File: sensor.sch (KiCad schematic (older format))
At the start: 91 parts, among them CON1 Micro USB, CON2 PROG, CON3 Jack-DC, CON4 HTU21D, CON5 Conn_01x08, Q1 BSS214N, Q2 BSS214N, Q3 BSS214N, Q4 BSS214N, Q5 BSS214N, Q6 BSS214N, SW1 RESET, SW2 CFG, U1 LM7805, U2 TLV1117LV33DCY, U3 ESP-12F, U4 HTU21D, U5 PMS7003

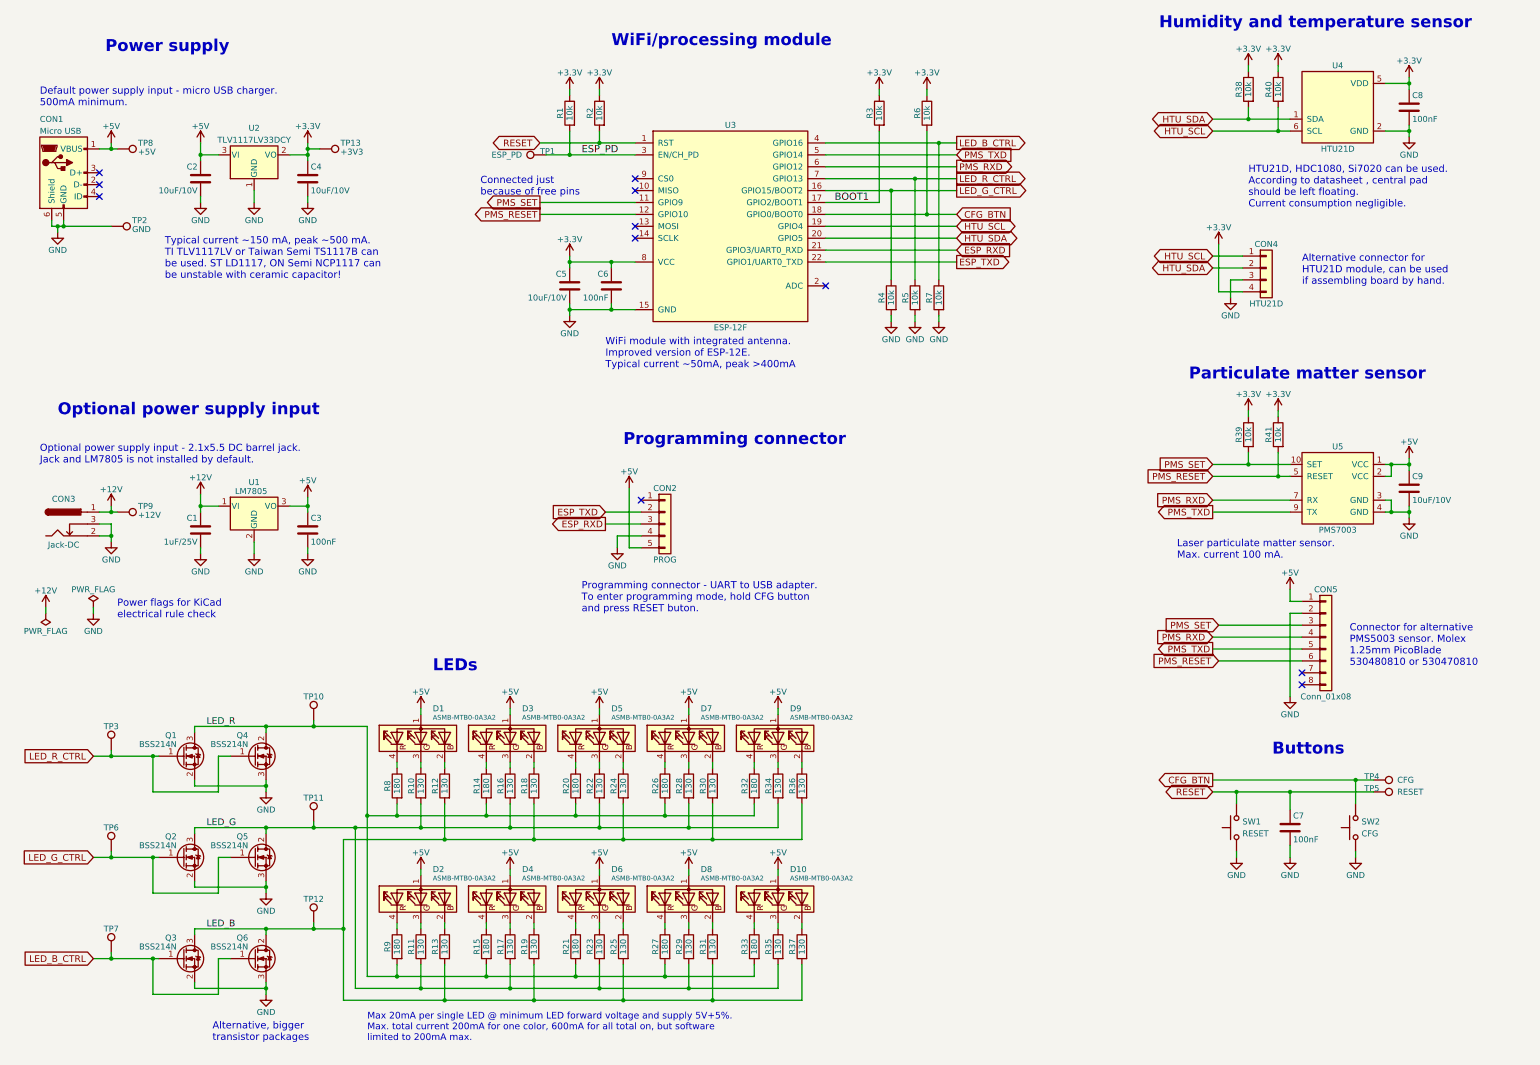
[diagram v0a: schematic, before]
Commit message: Add HTU21D module footprint
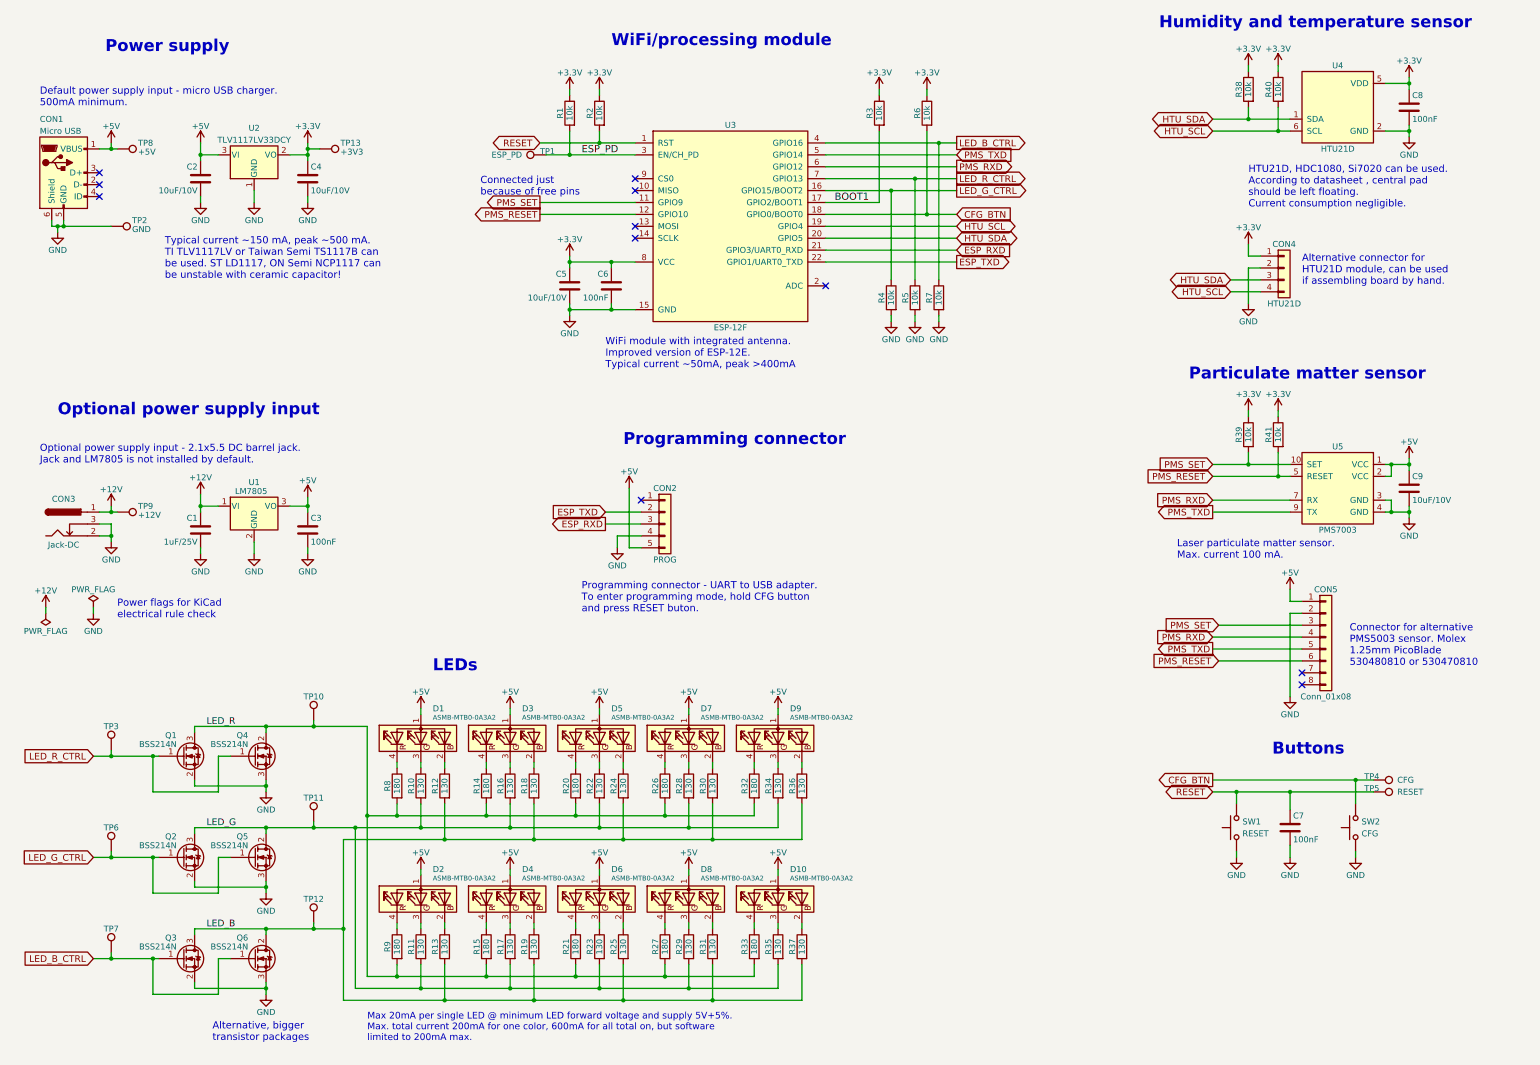
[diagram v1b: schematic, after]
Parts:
- CON4: footprint Pin_Headers:Pin_Header_Straight_1x04_Pitch2.54mm -> less-smog:HTU21D_module
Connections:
- net +3V3: now also CON4.1 (Pin_1); no longer CON4.4 (Pin_4)
- net GND: now also CON4.2 (Pin_2); no longer CON4.3 (Pin_3)
- net HTU_SCL: now also CON4.4 (Pin_4); no longer CON4.1 (Pin_1)
- net HTU_SDA: now also CON4.3 (Pin_3); no longer CON4.2 (Pin_2)
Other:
- moved on the sheet: CON4

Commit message: Change some footprints. Optimize routing.
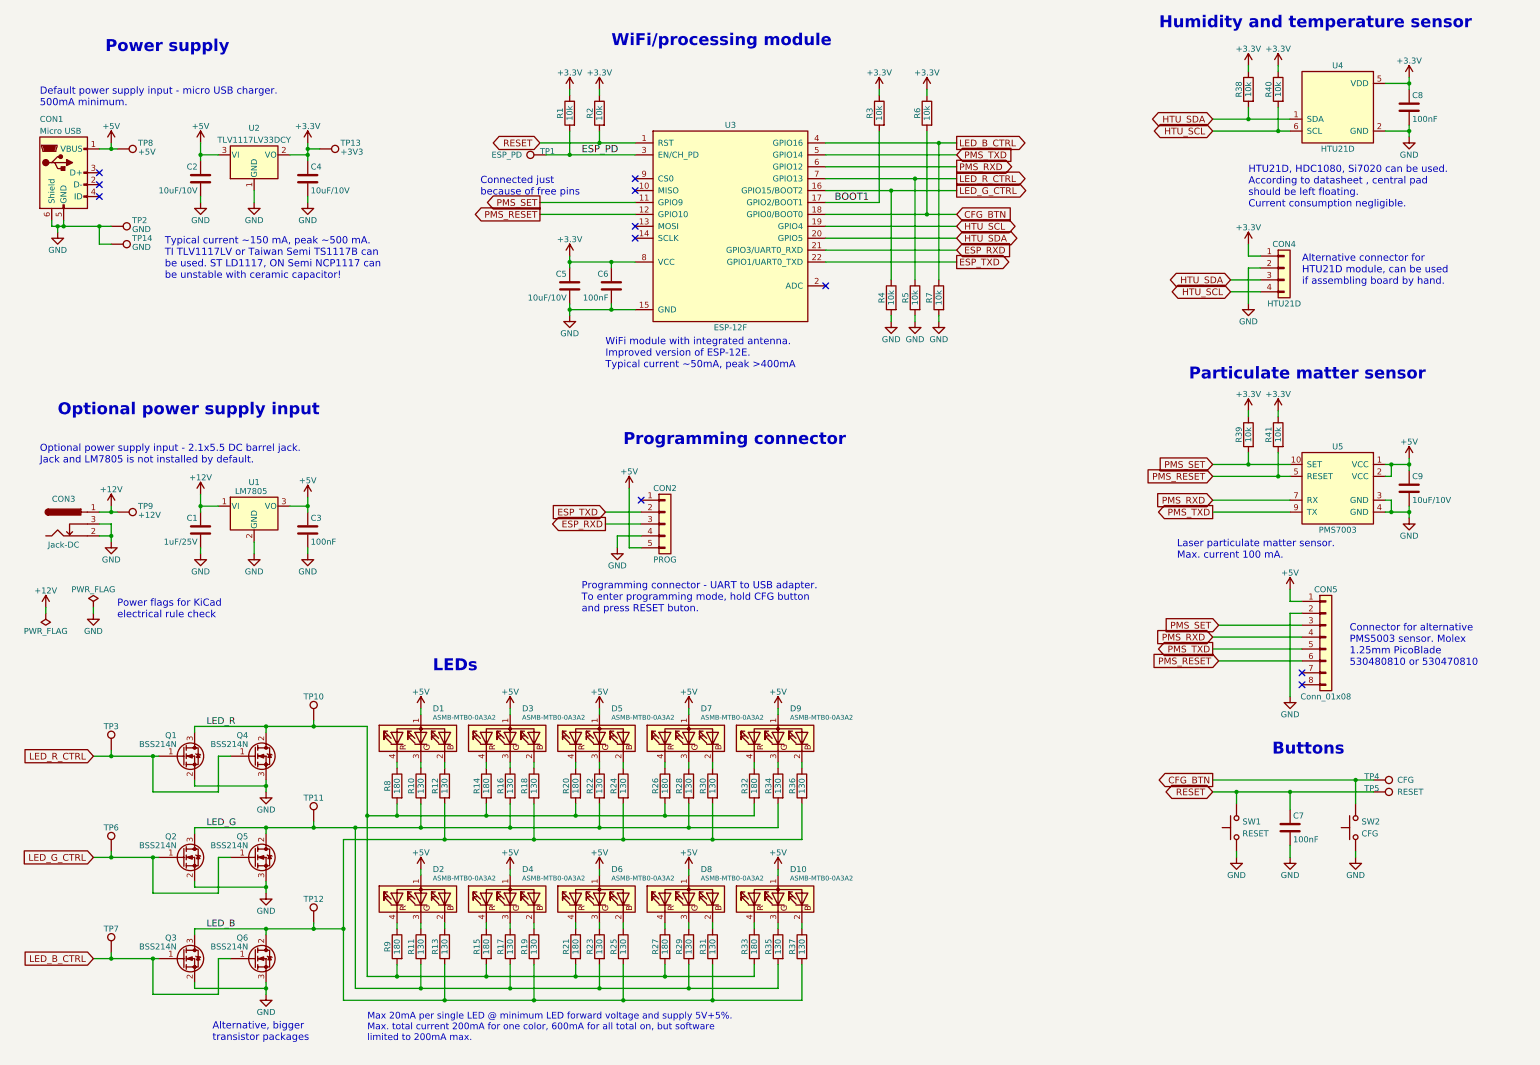
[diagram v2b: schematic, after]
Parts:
- added TP14: GND, less-smog:TP_1.7_1.0_THT, symbol TEST_1P
- CON2: footprint Pin_Headers:Pin_Header_Straight_1x05_Pitch2.54mm -> less-smog:Pin_Header_Straight_1x05_Pitch2.54mm
- TP1, TP10, TP11, TP12, TP13, TP3, TP6, TP7, TP8, TP9: footprint Wire_Pads:SolderWirePad_single_0-8mmDrill -> less-smog:TP_1.0_0.5_THT
- TP2, TP4, TP5: footprint Wire_Pads:SolderWirePad_single_0-8mmDrill -> less-smog:TP_1.7_1.0_THT
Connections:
- net GND: now also TP14.1

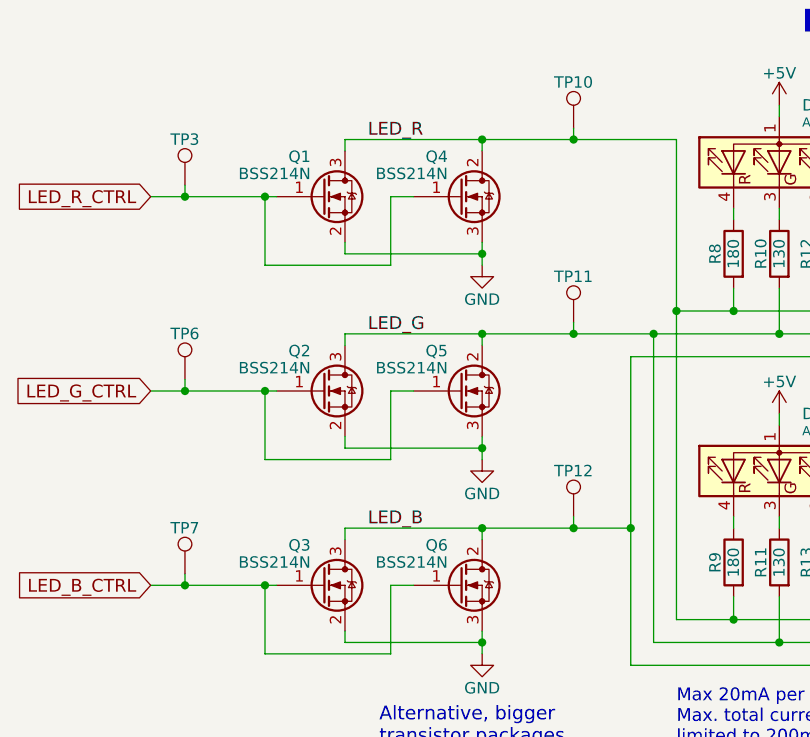
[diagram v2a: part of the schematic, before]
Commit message: Update assembly drawing and generate pdf. Fix alternative Q4..Q6 values.
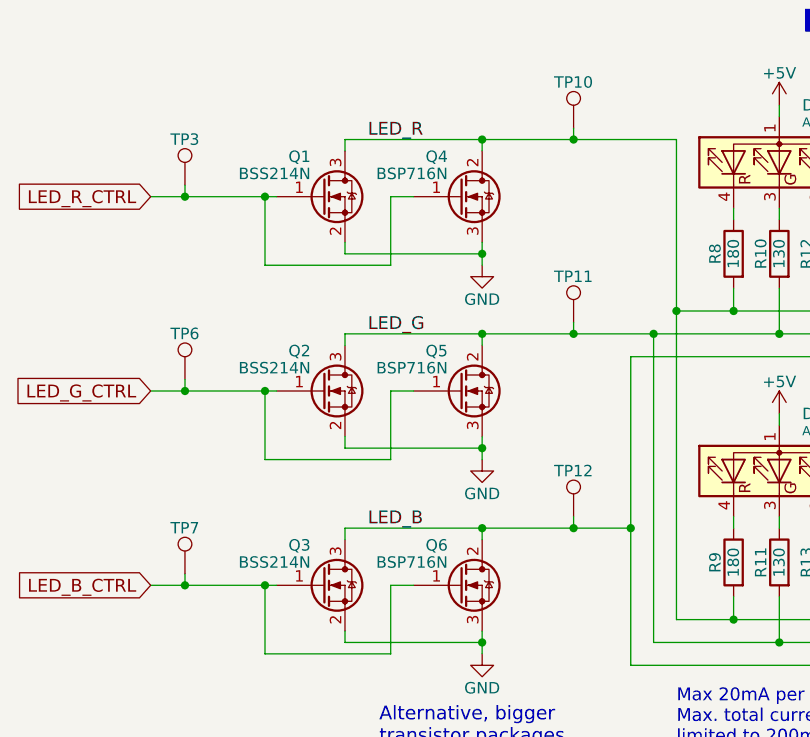
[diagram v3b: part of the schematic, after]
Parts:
- Q4, Q5, Q6: value BSS214N -> BSP716N
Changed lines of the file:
@@
 Data
 89 50 4E 47 0D 0A 1A 0A 00 00 00 0D 49 48 44 52 00 00 01 F4 00 00 00 AD 08 02 00 00 00 C9 42 1A
-56 00 00 00 03 73 42 49 54 08 08 08 DB E1 4F E0 00 00 00 09 70 48 59 73 00 00 2E 23 00 00 2E 23
-01 78 A5 3F 76 00 00 20 00 49 44 41 54 78 9C EC BD 69 AF 24 D9 91 25 76 CC EC 5E 77 8F 78 FB CB
+56 00 00 00 03 73 42 49 54 08 08 08 DB E1 4F E0 00 00 00 09 70 48 59 73 00 00 2E 18 00 00 2E 18
+01 2A AA 27 20 00 00 20 00 49 44 41 54 78 9C EC BD 69 AF 24 D9 91 25 76 CC EC 5E 77 8F 78 FB CB
 B5 76 2E 45 36 D9 0B BB 45 8C 1A D2 60 30 6A E9 93 FE 80 7E E6 00 02 04 7D 1A 0C 30 82 84 16 BA
 A7 D9 CD 66 B3 B9 17 6B CB AA AC DC DF 1A 11 EE 7E CD 8E 3E 5C 8F C8 C8 AD 58 64 17 29 26 99 56
@@
 P 2800 6850
 F 0 "Q4" H 2750 7025 50  0000 R CNN
-F 1 "BSS214N" H 2750 6950 50  0000 R CNN
+F 1 "BSP716N" H 2750 6950 50  0000 R CNN
 F 2 "TO_SOT_Packages_SMD:SOT-223-3Lead_TabPin2" H 3000 6950 50  0001 C CNN
 F 3 "" H 2800 6850 50  0001 C CNN
@@
 P 2800 7700
 F 0 "Q5" H 2750 7875 50  0000 R CNN
-F 1 "BSS214N" H 2750 7800 50  0000 R CNN
+F 1 "BSP716N" H 2750 7800 50  0000 R CNN
 F 2 "TO_SOT_Packages_SMD:SOT-223-3Lead_TabPin2" H 3000 7800 50  0001 C CNN
 F 3 "" H 2800 7700 50  0001 C CNN
@@
 P 2800 8550
 F 0 "Q6" H 2750 8725 50  0000 R CNN
-F 1 "BSS214N" H 2750 8650 50  0000 R CNN
+F 1 "BSP716N" H 2750 8650 50  0000 R CNN
 F 2 "TO_SOT_Packages_SMD:SOT-223-3Lead_TabPin2" H 3000 8650 50  0001 C CNN
 F 3 "" H 2800 8550 50  0001 C CNN

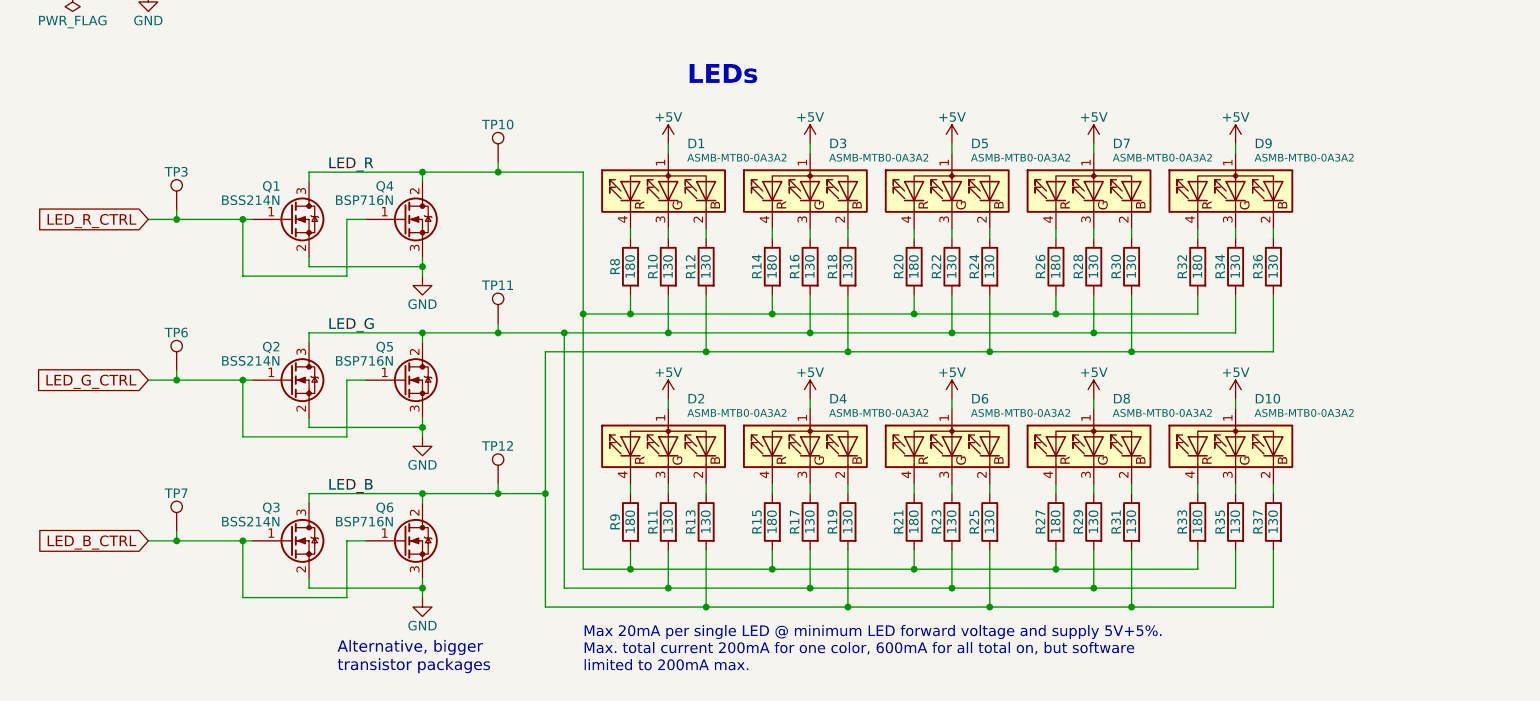
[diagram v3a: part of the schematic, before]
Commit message: [#4] Change LEDs to 5mm THT on schematic.
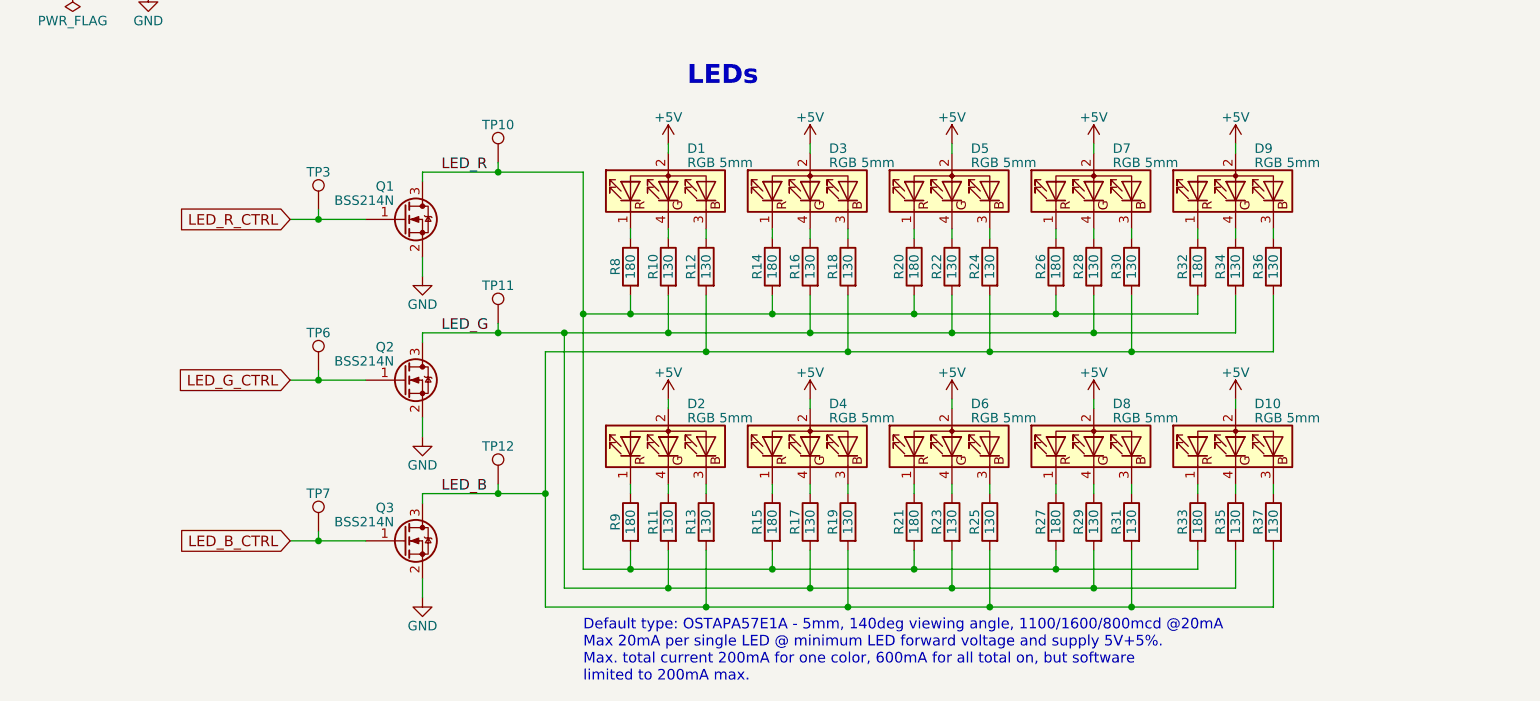
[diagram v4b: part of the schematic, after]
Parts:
- removed D1, D10, D2, D3, D4, D5, D6, D7, D8, D9: ASMB-MTB0-0A3A2, less-smog:ASMB-MTB0-0A3A2, symbol ASMB-MTB0-0A3A2
- removed Q4, Q5, Q6: BSP716N, TO_SOT_Packages_SMD:SOT-223-3Lead_TabPin2, symbol Q_NMOS_GDS
- added D1, D10, D2, D3, D4, D5, D6, D7, D8, D9: RGB 5mm, LEDs:LED_D5.0mm-4, symbol LED_RABG
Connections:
- net +5V: now also D1.2 (A), D10.2 (A), D2.2 (A), D3.2 (A), D4.2 (A), D5.2 (A), D6.2 (A), D7.2 (A), D8.2 (A), D9.2 (A)
- net at R12.1: now also D1.3 (BK)
- net at R10.1: now also D1.4 (GK)
- net at R8.1: now also D1.1 (RK)
- net at R18.1: now also D3.3 (BK)
- net at R16.1: now also D3.4 (GK)
- net at R14.1: now also D3.1 (RK)
- net at R24.1: now also D5.3 (BK)
- net at R22.1: now also D5.4 (GK)
- net at R20.1: now also D5.1 (RK)
- net at R36.1: now also D9.3 (BK)
- net at R34.1: now also D9.4 (GK)
- net at R32.1: now also D9.1 (RK)
- net at R30.1: now also D7.3 (BK)
- net at R28.1: now also D7.4 (GK)
- net at R26.1: now also D7.1 (RK)
- net at R13.1: now also D2.3 (BK)
- net at R11.1: now also D2.4 (GK)
- net at R9.1: now also D2.1 (RK)
- net at R19.1: now also D4.3 (BK)
- net at R17.1: now also D4.4 (GK)
- net at R15.1: now also D4.1 (RK)
- net at R25.1: now also D6.3 (BK)
- net at R23.1: now also D6.4 (GK)
- net at R21.1: now also D6.1 (RK)
- net at R37.1: now also D10.3 (BK)
- net at R35.1: now also D10.4 (GK)
- net at R33.1: now also D10.1 (RK)
- net at R31.1: now also D8.3 (BK)
- net at R29.1: now also D8.4 (GK)
- net at R27.1: now also D8.1 (RK)
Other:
- note added: "Default type: OSTAPA57E1A - 5mm, 140deg viewing angle, 1100/1600/800mcd @20mA\nMax 20mA per single LED @ minimum LED forward voltage and supply 5V+5%.\nMax. total current 200mA for one color, 600mA for all total on, but software\nlimited to 200mA max."
- note removed: "Alternative, bigger\ntransistor packages"
- note removed: "Max 20mA per single LED @ minimum LED forward voltage and supply 5V+5%.\nMax. total current 200mA for one color, 600mA for all total on, but software\nlimited to 200mA max."
- moved on the sheet: Q1, Q2, Q3, TP3, TP6, TP7
